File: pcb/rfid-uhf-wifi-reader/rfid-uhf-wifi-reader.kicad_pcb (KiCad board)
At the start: 2 copper layers, 15 parts, among them P1 USB_C_Plug, Q1 BSS138, Q2 BSS138, SW1 SW_Push, SW2 SW_Push, U1 ESP32-WROOM-32, U2 AMS1117-3.3, U3 CH340E

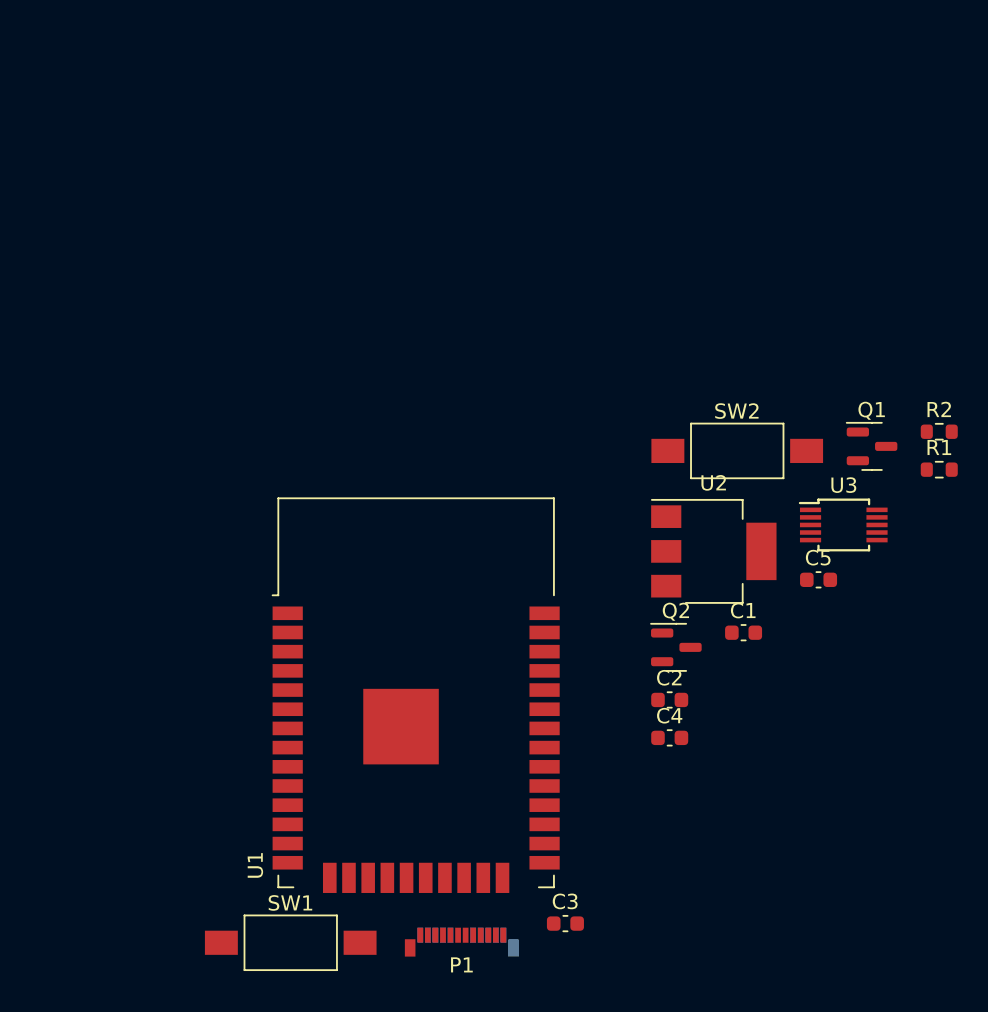
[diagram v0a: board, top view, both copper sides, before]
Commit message: place components
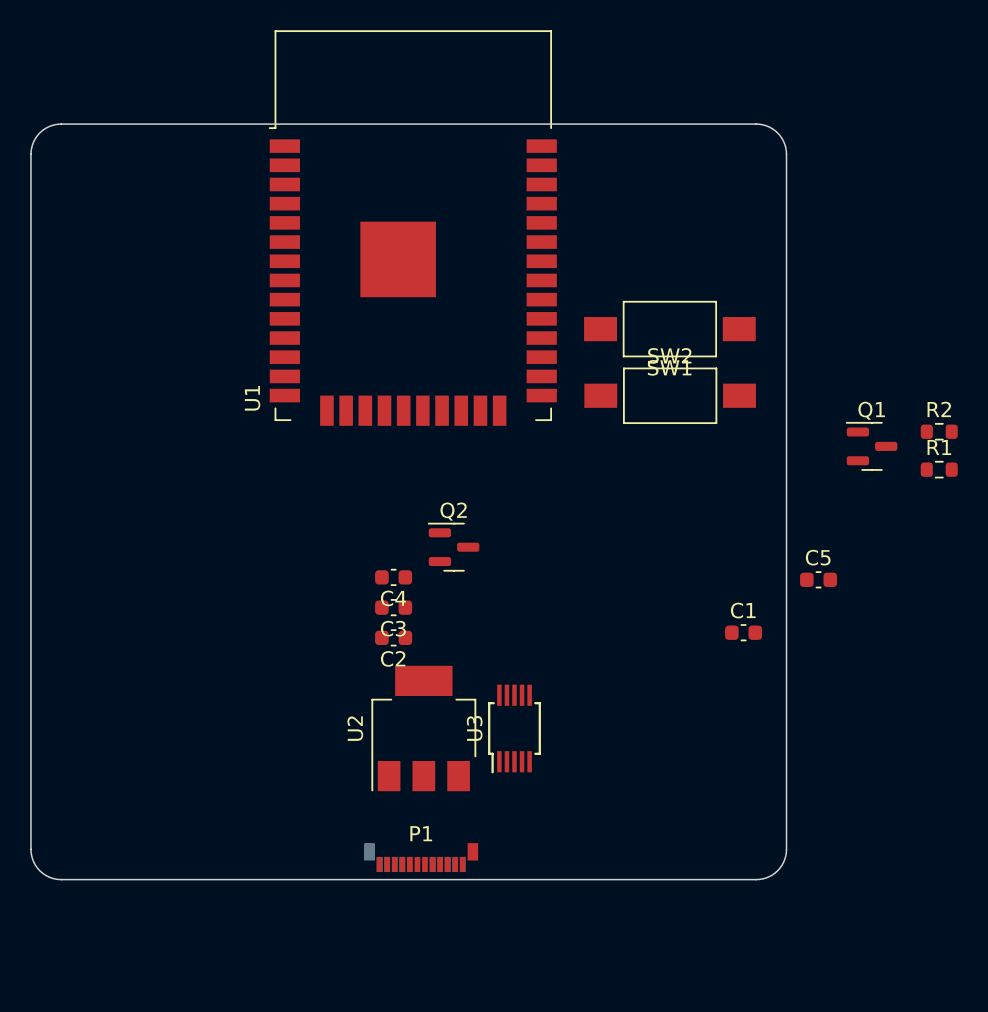
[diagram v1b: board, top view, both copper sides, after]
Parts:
- moved SW1 47.7 mm to (132.3, 53.6), turned to 180 degrees
- moved U1 30.9 mm to (115.3, 49.7)
- moved U3 25.6 mm to (122.0, 80.0), turned to 90 degrees
- moved C3 23.8 mm to (114.0, 72.0), turned to 180 degrees
- moved U2 22.5 mm to (116.0, 80.0), turned to 90 degrees
- moved C4 21.1 mm to (114.0, 70.0), turned to 180 degrees
- moved C2 18.7 mm to (114.0, 74.0), turned to 180 degrees
- moved Q2 16.1 mm to (118.0, 68.0)
- moved SW2 5.75 mm to (132.3, 58.0)
- moved P1 5.33 mm to (115.8, 89.0), turned to 180 degrees
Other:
- board outline added: 50 x 50 mm

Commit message: place components
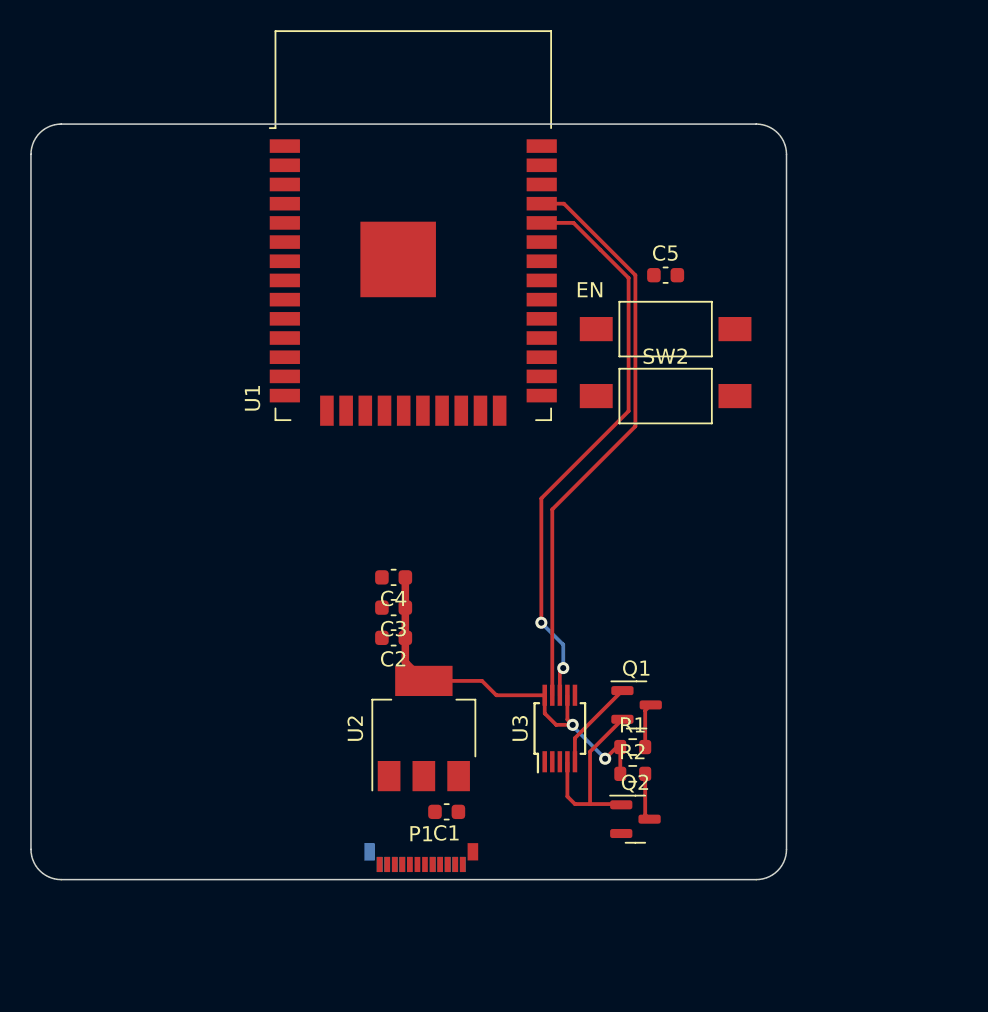
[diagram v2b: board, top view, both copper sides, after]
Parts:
- moved R2 30.4 mm to (129.8, 83.0)
- moved R1 27.4 mm to (129.8, 81.2)
- moved Q1 23.1 mm to (130.1, 78.4)
- moved C1 22.9 mm to (117.5, 85.5), turned to 180 degrees
- moved C5 22.6 mm to (132.0, 50.0)
- moved Q2 21.6 mm to (130.0, 86.0)
- moved U3 3.00 mm to (125.0, 80.0)
- moved SW2 0.30 mm to (132.0, 58.0)
- moved EN 0.28 mm to (132.0, 53.6)
- renumbered SW1 to EN
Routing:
- net RX-PROG: track 0.00 -> 38.2 mm
- net TX-PROG: track 0.00 -> 38.0 mm, vias 0 -> 2
- net +3V3: track 0.00 -> 27.4 mm, vias 0 -> 2
- net Net-(Q1-Pad2): track 0.00 -> 12.6 mm
- net Net-(Q1-Pad1): track 0.00 -> 6.01 mm
- net ESP32_IO0: track 0.00 -> 3.12 mm
- net ESP32_EN: track 0.00 -> 2.94 mm

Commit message: update components
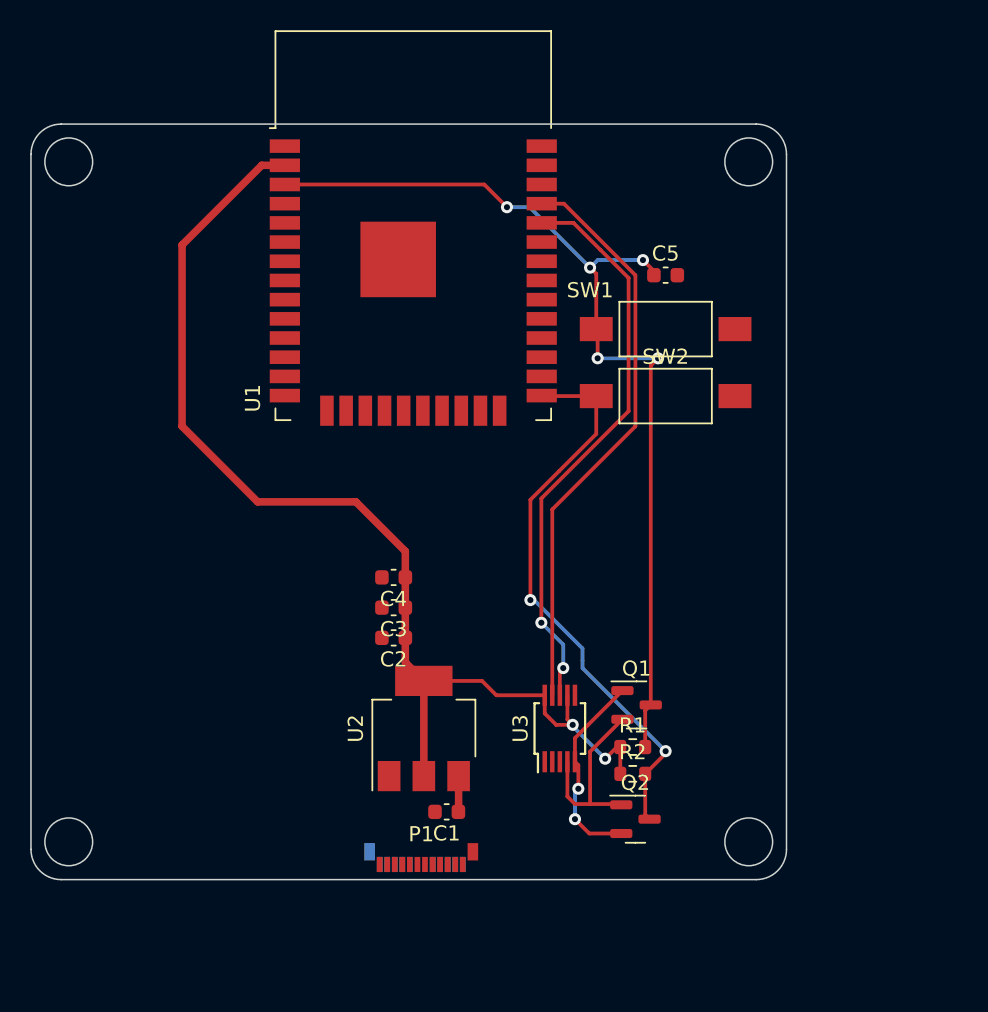
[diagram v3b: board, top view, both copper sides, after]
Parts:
- renumbered EN to SW1
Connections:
- U1 pad 2: unconnected-(U1-Pad2) -> +3V3
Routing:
- net ESP32_EN: track 2.94 -> 63.8 mm, vias 0 -> 5
- net +3V3: track 27.4 -> 74.7 mm
- net ESP32_IO0: track 3.12 -> 38.0 mm, vias 0 -> 2
- net Net-(Q1-Pad1): track 6.01 -> 13.5 mm, vias 0 -> 2
- net +5V: track 0.00 -> 2.37 mm
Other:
- outline, holes or cut-outs redrawn

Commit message: add rfid connector
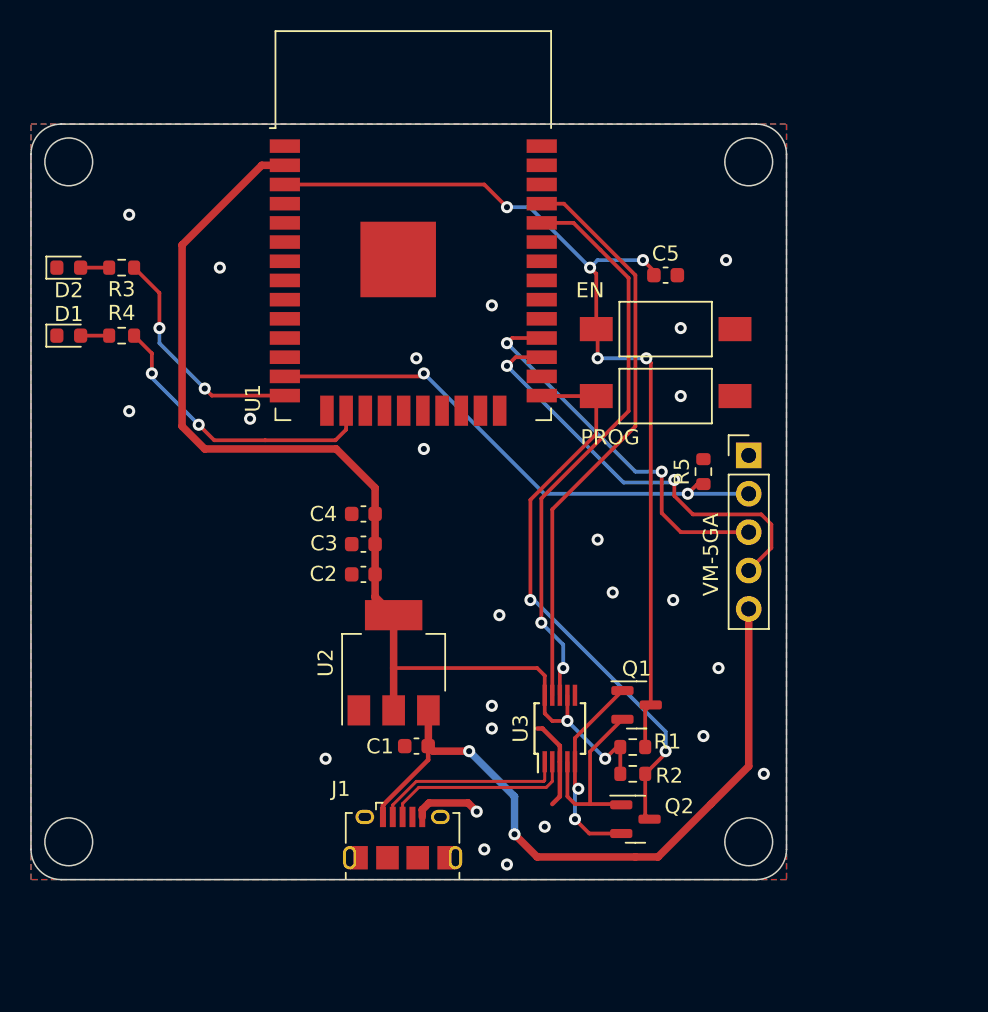
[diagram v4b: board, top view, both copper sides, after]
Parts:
- removed P1: USB_C_Plug, Connector_USB:USB_C_Plug_Molex_105444
- added D1: LED, LED_SMD:LED_0603_1608Metric, F.Cu at (92.5, 54.0)
- added D2: LED, LED_SMD:LED_0603_1608Metric, F.Cu at (92.5, 49.5)
- added J1: USB_OTG, Connector_USB:USB_Micro-B_Amphenol_10118194_Horizontal, F.Cu at (114.6, 87.3)
- added R3: R_Small, Resistor_SMD:R_0603_1608Metric, F.Cu at (96.0, 49.5)
- added R4: R_Small, Resistor_SMD:R_0603_1608Metric, F.Cu at (96.0, 54.0)
- added R5: R_Small, Resistor_SMD:R_0603_1608Metric, F.Cu at (134.5, 63.0)
- added VM-5GA: Conn_01x05, Connector_PinHeader_2.54mm:PinHeader_1x05_P2.54mm_Vertical, F.Cu at (137.5, 61.9)
- moved C1 4.79 mm to (115.5, 81.2)
- moved U2 4.79 mm to (114.0, 75.7)
- moved C2 4.65 mm to (112.0, 69.8)
- moved C3 4.65 mm to (112.0, 67.8)
- moved C4 4.65 mm to (112.0, 65.8)
- renumbered SW1 to EN, SW2 to PROG
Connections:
- U1 pad 1: Net-(U1-Pad1) -> GND
- U1 pad 13: unconnected-(U1-Pad13) -> VM-EN
- U1 pad 14: unconnected-(U1-Pad14) -> Net-(U1-Pad14)
- U1 pad 15: Net-(U1-Pad1) -> GND
- U1 pad 16: unconnected-(U1-Pad16) -> Net-(U1-Pad16)
- U1 pad 27: unconnected-(U1-Pad27) -> VM-TX
- U1 pad 28: unconnected-(U1-Pad28) -> VM-RX
- U1 pad 38: Net-(U1-Pad1) -> GND
- U1 pad 39: Net-(U1-Pad1) -> GND
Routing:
- net +5V: track 2.37 -> 46.9 mm, vias 0 -> 2
- net VM-EN: track 0.00 -> 35.4 mm, vias 0 -> 2
- net VM-TX: track 0.00 -> 28.8 mm, vias 0 -> 2
- net VM-RX: track 0.00 -> 25.2 mm, vias 0 -> 2
- net Net-(U1-Pad16): track 0.00 -> 19.4 mm, vias 0 -> 2
- net Net-(U1-Pad14): track 0.00 -> 15.4 mm, vias 0 -> 2
- net D-: track 0.00 -> 12.8 mm
- net D+: track 0.00 -> 12.7 mm
- net GND: track 0.00 -> 10.5 mm, vias 0 -> 24
- net Net-(D2-Pad2): track 0.00 -> 1.89 mm
- net Net-(D1-Pad2): track 0.00 -> 1.89 mm
- net +3V3: track 74.7 -> 73.6 mm
- net ESP32_EN: track 63.8 -> 62.9 mm
- added copper zone on B.Cu, net GND
- added copper zone on F.Cu, net GND
